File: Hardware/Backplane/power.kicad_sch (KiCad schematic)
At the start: 59 parts, among them J901 Conn_01x05, U101 P2X8C4M64P, U901 AP3445LW6-7

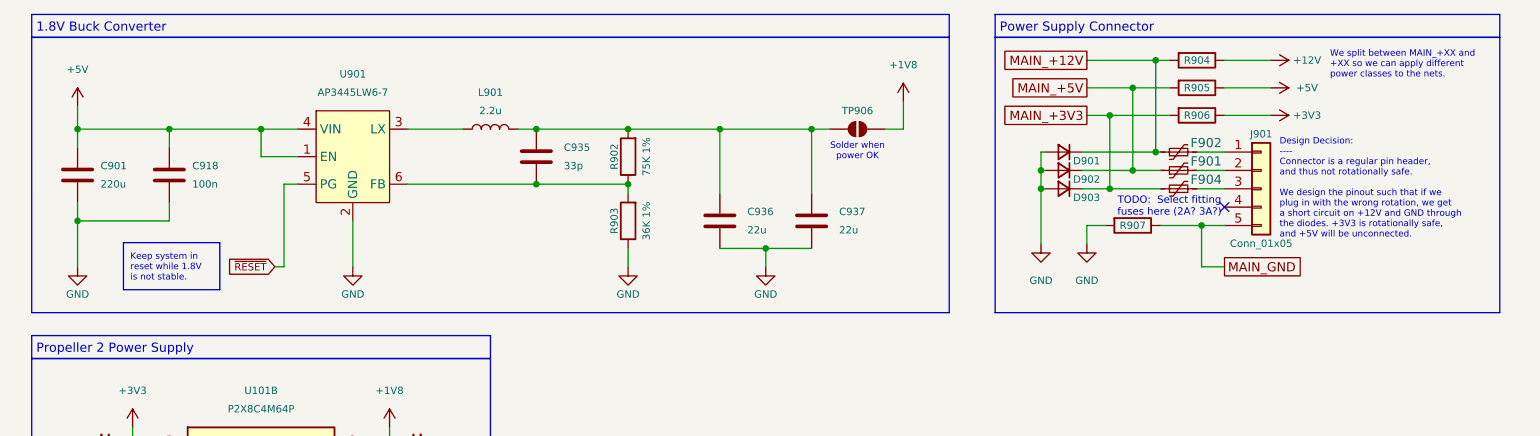
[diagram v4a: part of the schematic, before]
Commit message: Upgrades power-on reset system to be close to bullet-proof by having a power-good coupled mono flop that continues holding reset after PG goes high for some time
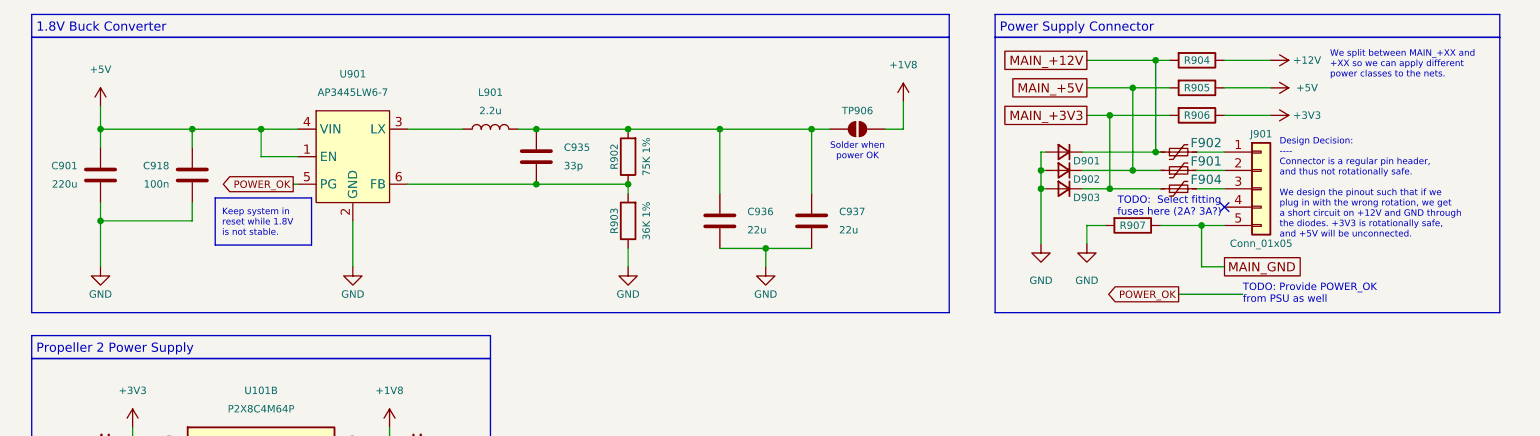
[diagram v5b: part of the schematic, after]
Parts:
- D901, D902, D903: value D_Small -> Something Short-Circuit Safe
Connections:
- net ~{RESET} renamed POWER_OK
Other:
- note added: "TODO: Provide POWER_OK from PSU as well"
- moved on the sheet: C901, C918

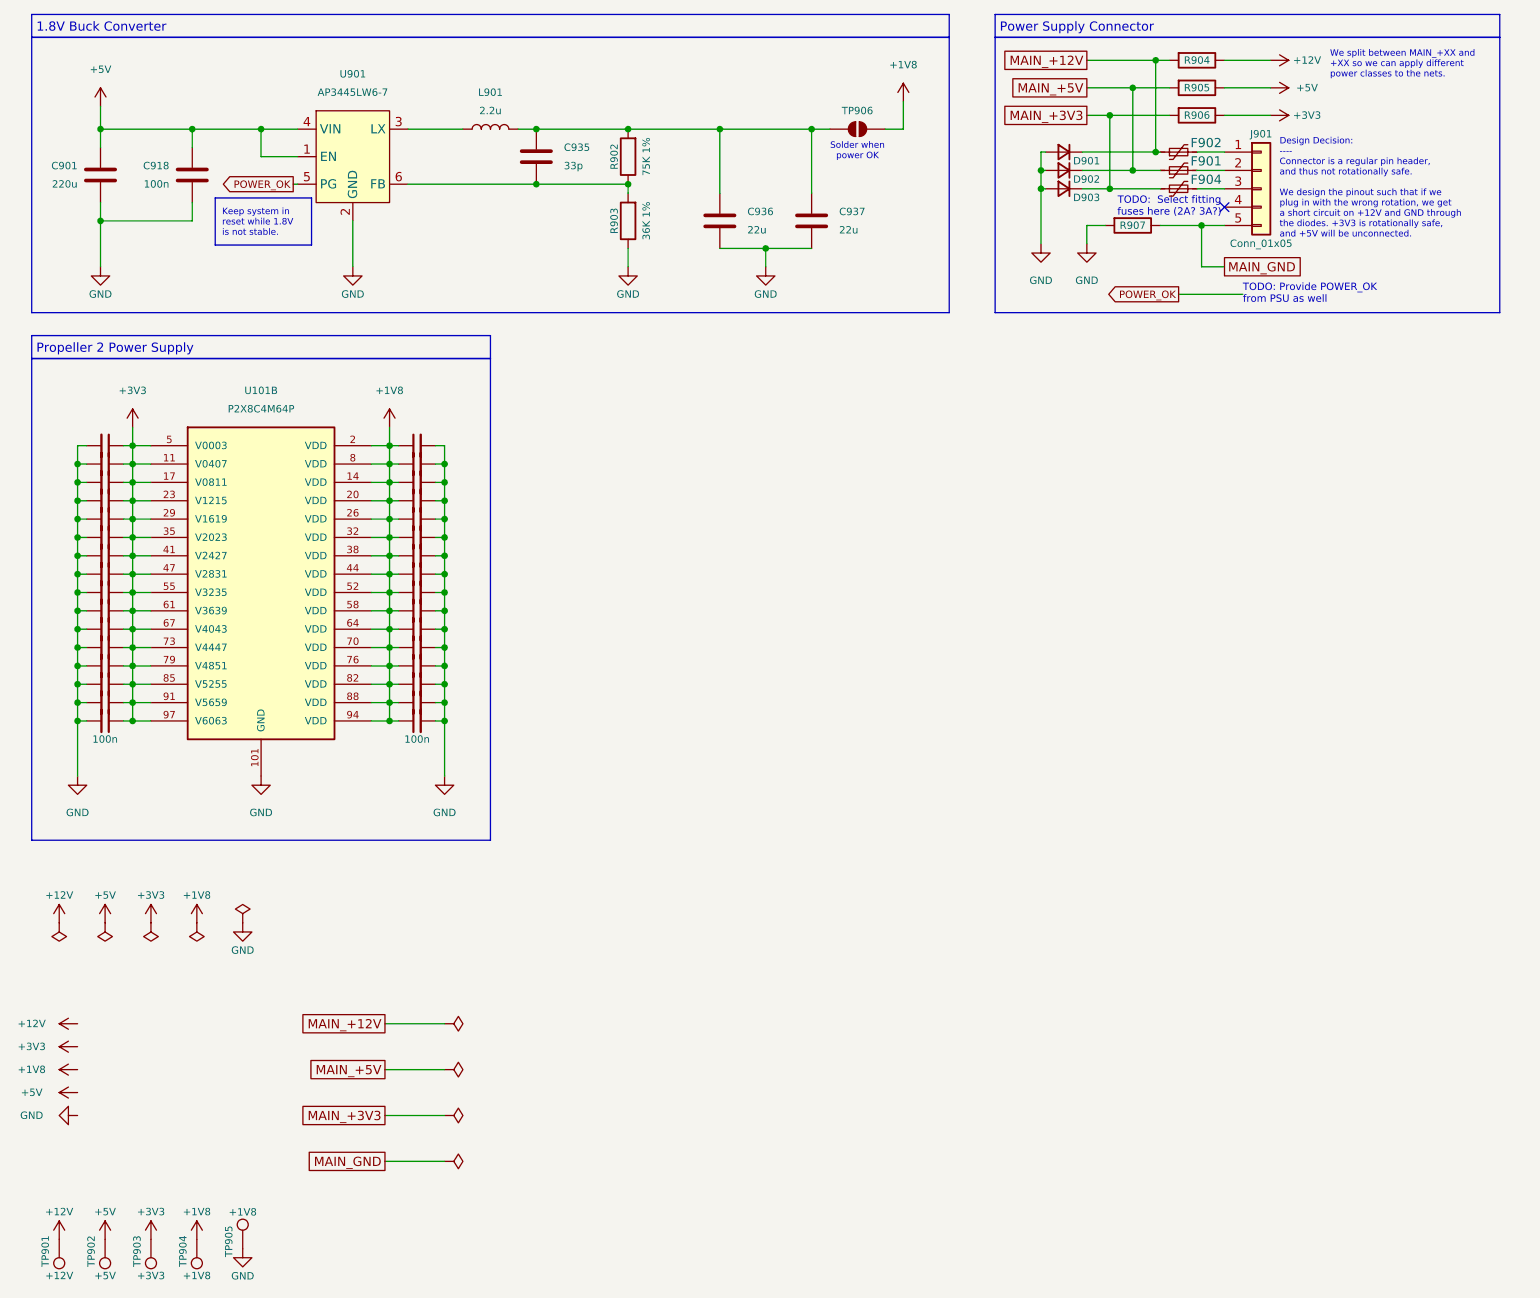
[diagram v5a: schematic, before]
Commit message: Refactors clock system to use AND gates for clock tree spanning and gating.
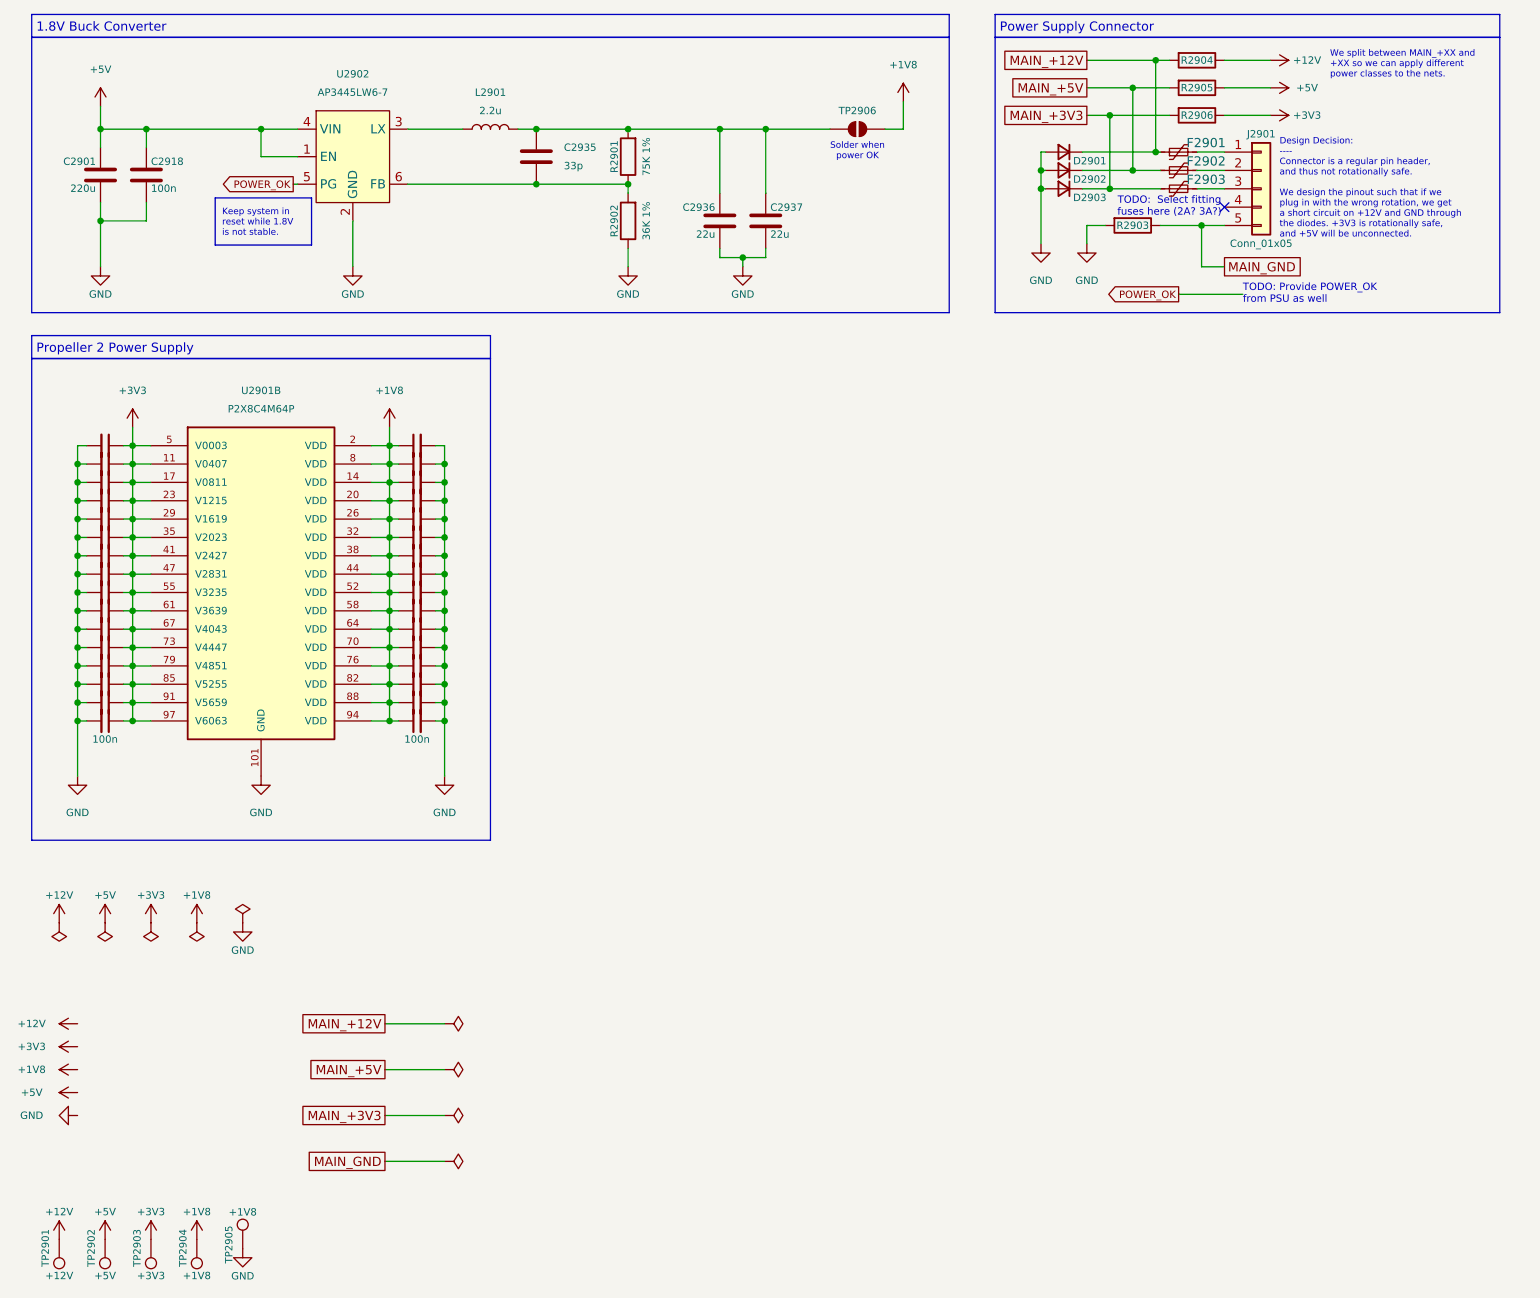
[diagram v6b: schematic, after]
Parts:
- removed F901, F904: SMD1206B050TF/15, symbol Symbol Library:SMD1206B050TF/15
- added F2901, F2903: SMD1206B050TF/15, symbol Symbol Library:SMD1206B050TF/15
- F2902: renamed from F902; Digikey Part No (none) -> 13-SMD1206B050TF/15TR-ND
- renumbered C901 to C2901, C902 to C2902, C903 to C2903, C904 to C2904, C905 to C2905, C906 to C2906, C907 to C2907, C908 to C2908, C909 to C2909, C910 to C2910, C911 to C2911, C912 to C2912, C913 to C2913, C914 to C2914, C915 to C2915, C916 to C2916, C917 to C2917, C918 to C2918, C919 to C2919, C920 to C2920, C921 to C2921, C922 to C2922, C923 to C2923, C924 to C2924, C925 to C2925, C926 to C2926, C927 to C2927, C928 to C2928, C929 to C2929, C930 to C2930, C931 to C2931, C932 to C2932, C933 to C2933, C934 to C2934, C935 to C2935, C936 to C2936, C937 to C2937, D901 to D2901, D902 to D2902, D903 to D2903, J901 to J2901, L901 to L2901, R902 to R2901, R903 to R2902, R907 to R2903, R904 to R2904, R905 to R2905, R906 to R2906, TP901 to TP2901, TP902 to TP2902, TP903 to TP2903, TP904 to TP2904, TP905 to TP2905, TP906 to TP2906, U101 to U2901, U901 to U2902
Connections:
- net MAIN_+12V: now also F2901.1; no longer F2902.1
- net MAIN_+3V3: now also F2903.1
- net MAIN_+5V: now also F2902.1
- net at F2902.2: now also J2901.2 (Pin_2); no longer J2901.1 (Pin_1)
- net at J2901.3 (Pin_3): now also F2903.2
- new net: F2901.2, J2901.1 (Pin_1)
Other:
- moved on the sheet: C2918, C2936, C2937, F2902

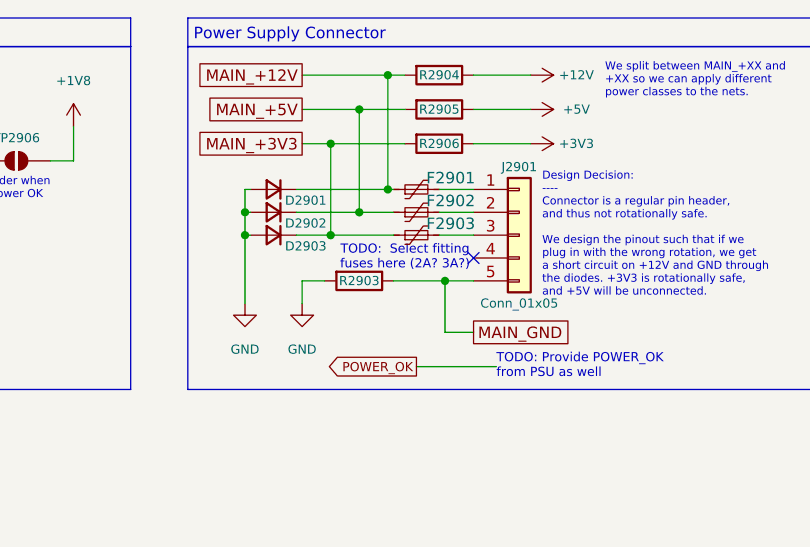
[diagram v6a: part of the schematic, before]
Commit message: Some cleanups of Backplane schematic: Adds DigiKey part numbers, removes unnecessary properties, marks test points as excluded from BOM
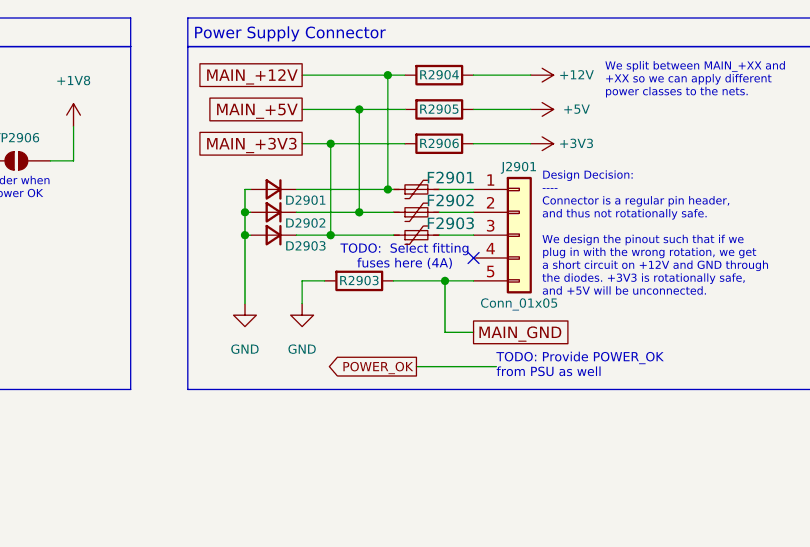
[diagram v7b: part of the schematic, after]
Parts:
- TP2901, TP2902, TP2903, TP2904, TP2905: now left out of the parts list
- U2901: Availability In Stock -> (none); Check_prices https://www.snapeda.com/parts/P2X8C4M64P/Parallax/view-part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 -> (none); Description_1 P2X8C4M64P Propeller™ Microcontroller IC 32-Bit 8-Core 180M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 -> (none); Digikey Part No (none) -> 149-P2X8C4M64P-ND; MANUFACTURER Parallax Inc. -> (none); MAXIMUM_PACKAGE_HEIGHT 1.2mm -> (none); MF Parallax Inc. -> (none); MP P2X8C4M64P -> (none); PARTREV 2022/11/01 -> (none); Package None -> (none); Price None -> (none); SNAPEDA_PN P2X8C4M64P -> (none); STANDARD IPC-7351B -> (none); SnapEDA_Link https://www.snapeda.com/parts/P2X8C4M64P/Parallax/view-part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 -> (none)
- U2902: Digikey Part No (none) -> AP3445LW6-7DICT-ND
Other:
- note added: "TODO: Select fitting fuses here (4A)"
- note removed: "TODO: Select fitting fuses here (2A? 3A?)"
